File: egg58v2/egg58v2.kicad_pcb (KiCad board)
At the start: 2 copper layers, 141.1 x 127.1 mm, 43 parts, among them J1 AudioJack4, SW11 SW_PUSH_LED, SW12 SW_PUSH_LED, SW13 SW_PUSH_LED, SW14 SW_PUSH_LED, SW15 SW_PUSH_LED, SW16 SW_PUSH_LED, SW21 SW_PUSH_LED, SW22 SW_PUSH_LED, SW23 SW_PUSH_LED, SW24 SW_PUSH_LED, SW25 SW_PUSH_LED, SW26 SW_PUSH_LED, SW31 SW_PUSH_LED, SW32 SW_PUSH_LED, SW33 SW_PUSH_LED, SW34 SW_PUSH_LED, SW35 SW_PUSH_LED, SW36 SW_PUSH_LED, SW41 SW_PUSH_LED, SW42 SW_PUSH_LED, SW43 SW_PUSH_LED, SW44 SW_PUSH_LED, SW45 SW_PUSH_LED, SW46 SW_PUSH_LED, SW52 SW_PUSH_LED, SW53 SW_PUSH_LED, SW54 SW_PUSH_LED, SW55 SW_PUSH_LED, SW56 SW_PUSH_LED, U1 Elite-C

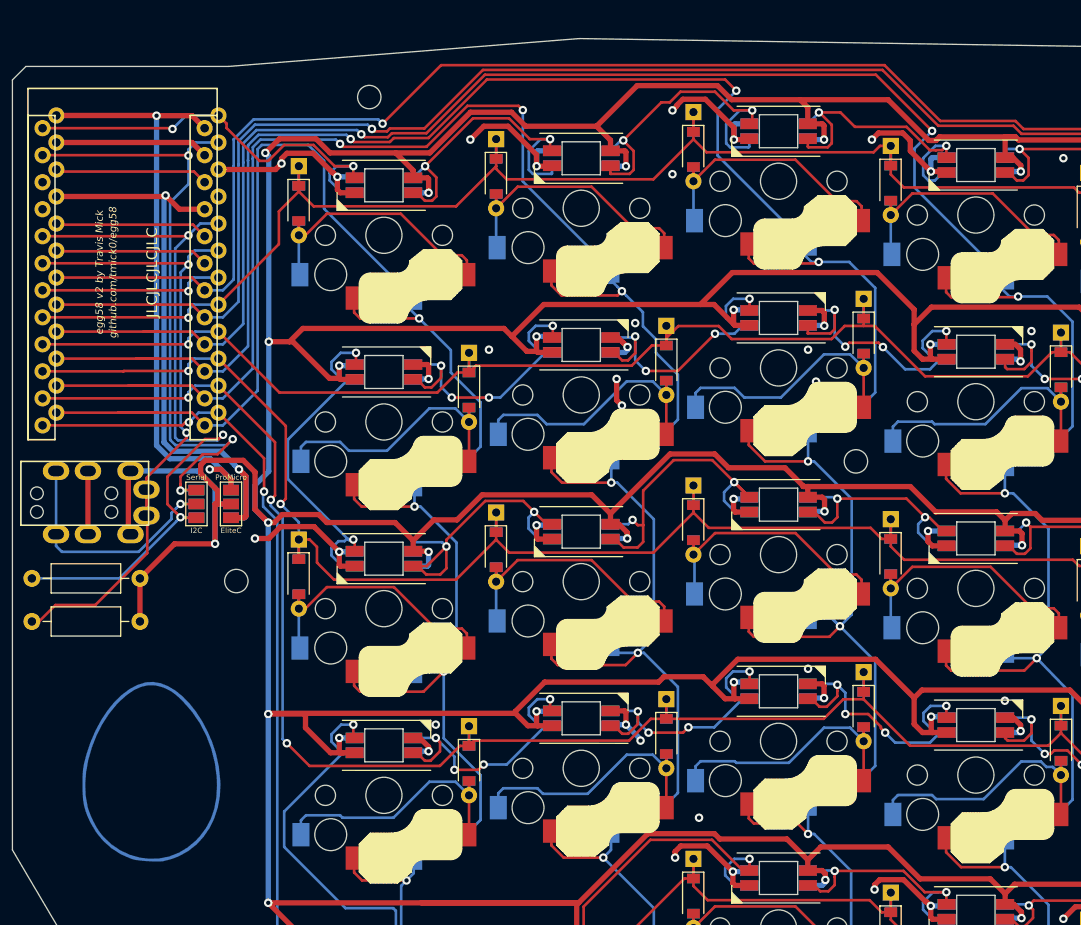
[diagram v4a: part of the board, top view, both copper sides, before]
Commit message: First draft of switchplate
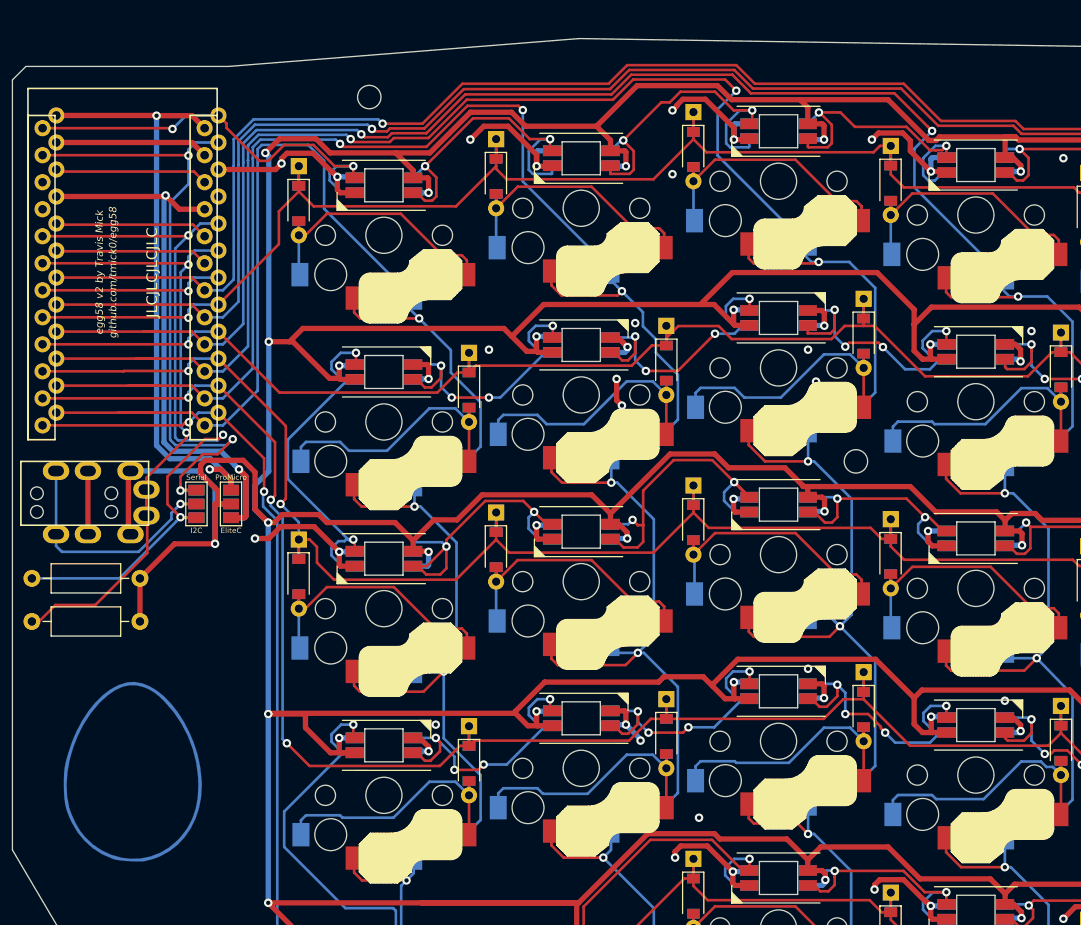
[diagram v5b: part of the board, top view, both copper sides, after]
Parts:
- removed the REF** at (129.0, 87.8)
- moved G*** 1.75 mm to (119.2, 105.8)

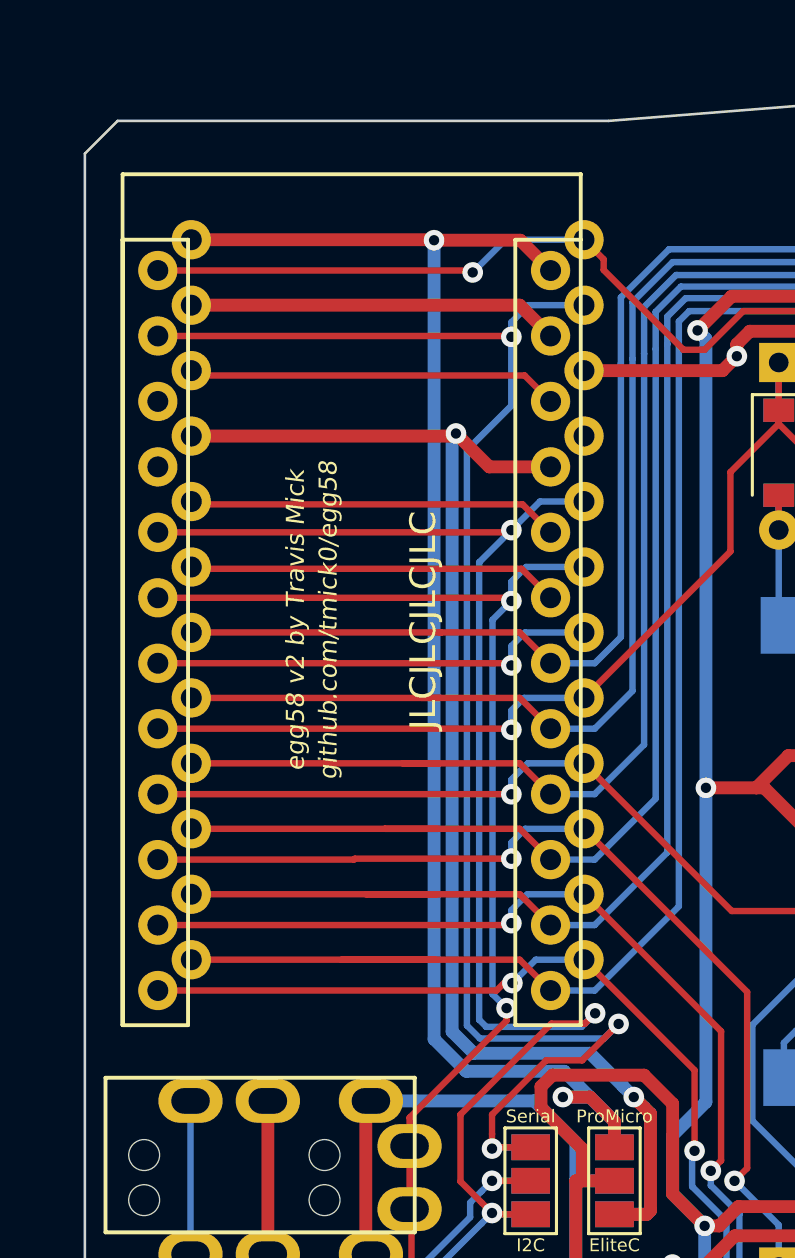
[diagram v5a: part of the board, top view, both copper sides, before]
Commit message: Add support for VBUS from EliteC
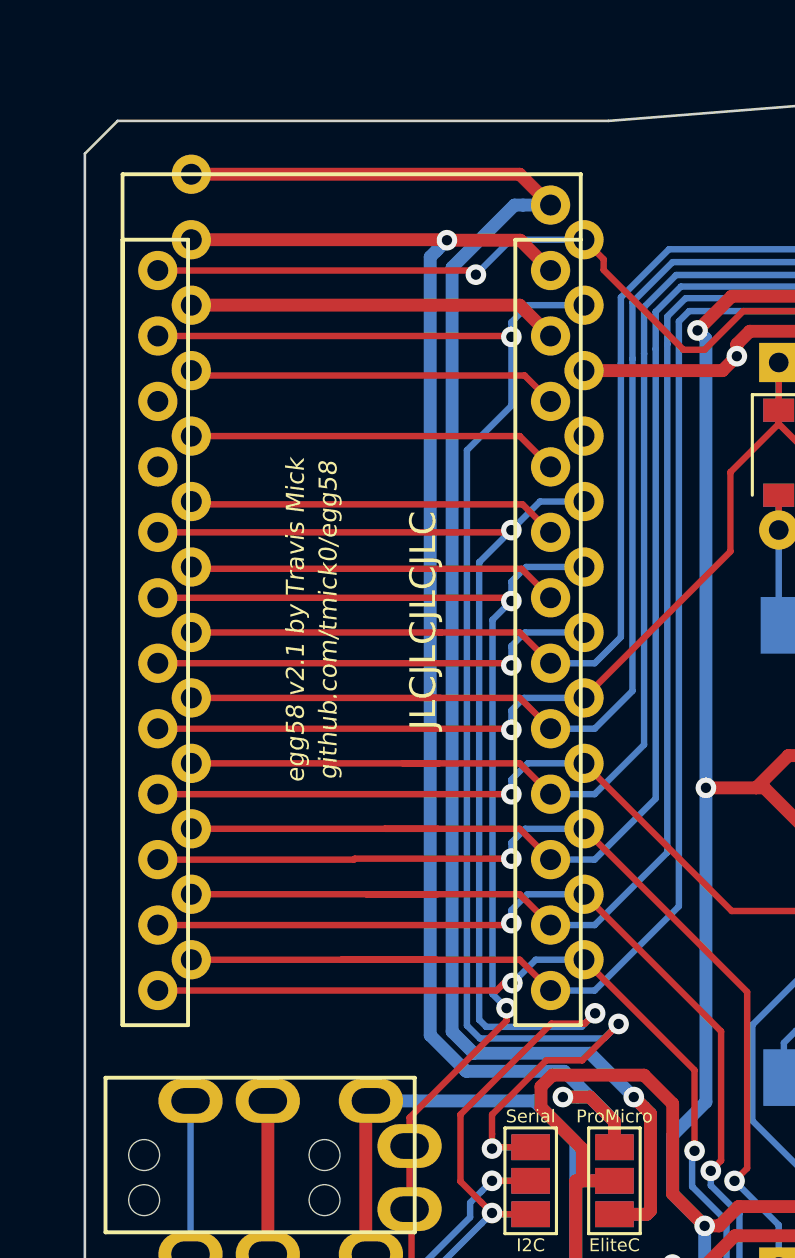
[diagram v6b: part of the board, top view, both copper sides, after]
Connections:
- U1 pad 21: VREG -> Net-(U1-Pad21)
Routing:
- net Net-(U1-Pad21): track 0.00 -> 14.4 mm
- net VREG: track 58.2 -> 69.3 mm, vias 2 -> 1
